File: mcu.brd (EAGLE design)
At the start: 36.7 x 57.5 mm, 64 parts, among them IC1 MCP73831/OT, T1 SI7051-A20, U4 NRF52832, U7 CP2102N-A01-GQFN24, X1 LFXTAL069526, X6 32.768kHz

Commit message: UPD: finishied version to macrofab
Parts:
- removed GND: (no value), microbuilder:TESTPOINT_ROUND_2MM
- moved C42 10.2 mm to (48.8, 43.6), turned to 0 degrees
- moved R9 8.40 mm to (46.0, 64.1), turned to 0 degrees
- moved L10 7.43 mm to (46.0, 43.9)
- moved R11 6.39 mm to (46.0, 41.3)
- moved R15 4.80 mm to (46.0, 62.1), turned to 0 degrees
- moved L9 3.90 mm to (45.4, 46.4), turned to 270 degrees
- moved DFU 3.70 mm to (49.1, 64.3)
- moved R12 1.05 mm to (44.1, 54.0), turned to 90 degrees
- moved X6 0.89 mm to (48.2, 45.7)
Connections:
- net GND: no longer GND.P$1
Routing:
- net DEC4: track 4.97 -> 16.2 mm
- net P0.26: track 59.8 -> 68.2 mm
- net VBAT: track 43.9 -> 37.1 mm
- net P0.31: track 16.5 -> 20.3 mm
- net P0.25: track 61.9 -> 65.7 mm
- net N$10: track 5.60 -> 7.61 mm
- net P0.20: track 13.2 -> 12.4 mm
- net P0.01/XL2: track 5.94 -> 6.67 mm
- net V+: track 95.4 -> 94.7 mm
- net GND: vias 101 -> 103
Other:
- board size 36.7 x 57.5 mm -> 35.5 x 57 mm
- board text removed: "GND"

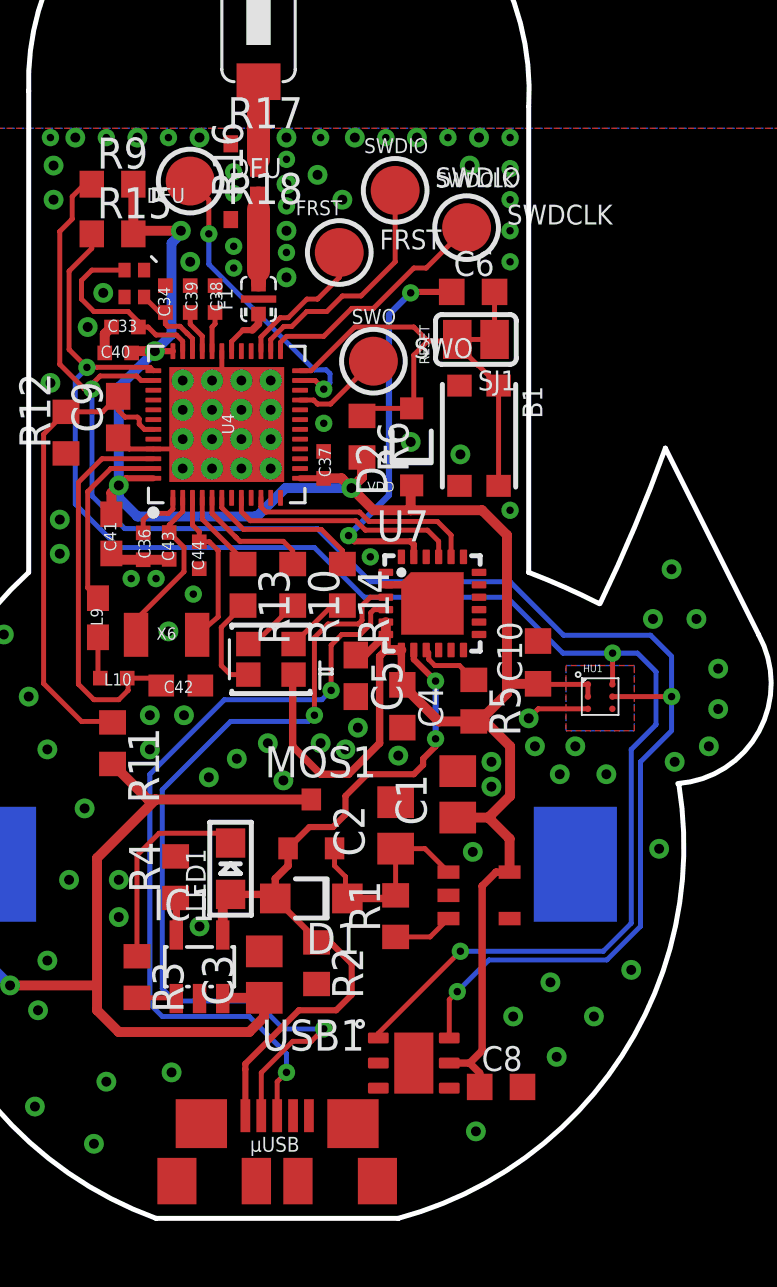
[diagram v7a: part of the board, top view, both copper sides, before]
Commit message: FIX: txd, rxd lines, usb. UPD: testpoints.
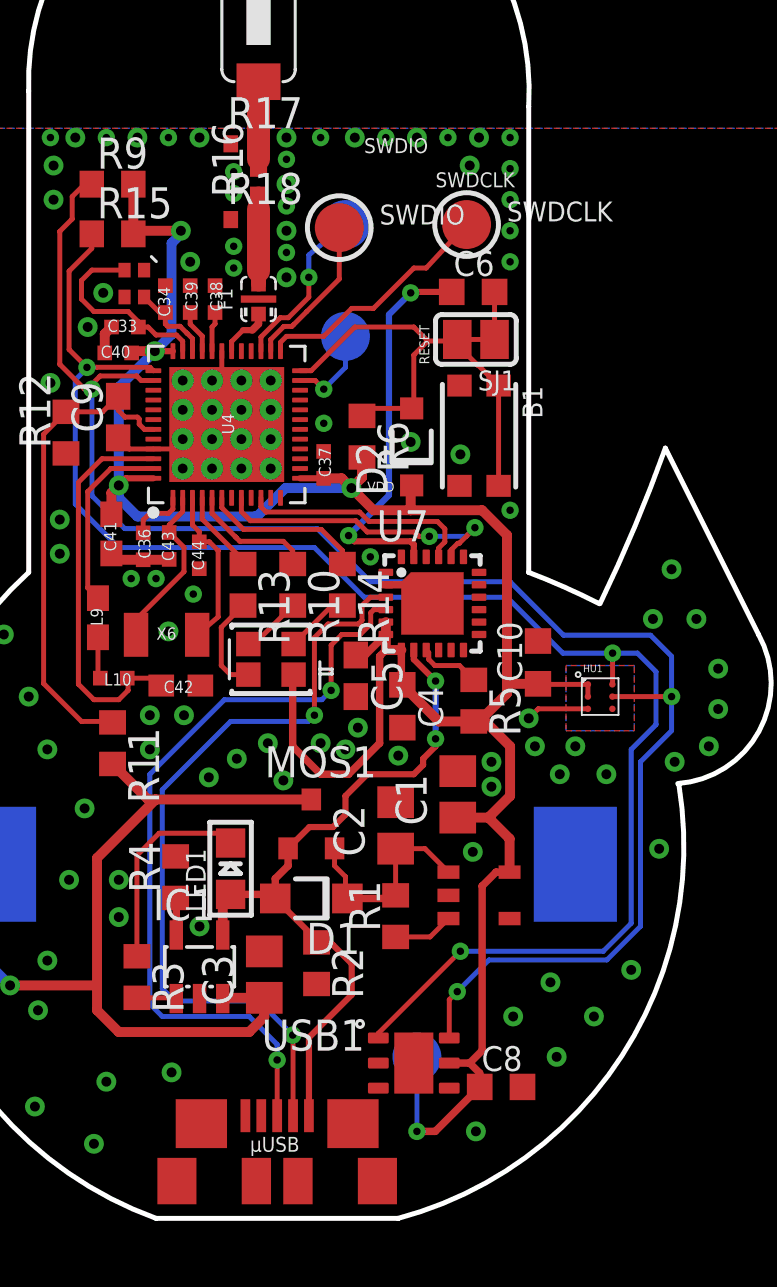
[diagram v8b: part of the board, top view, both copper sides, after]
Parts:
- moved SWO 28.5 mm to (58.4, 28.4), flipped to the bottom
- moved DFU 8.98 mm to (55.5, 57.9), flipped to the bottom
- moved SWDIO 2.75 mm to (55.2, 62.4)
- moved FRST 1.17 mm to (55.5, 62.5), flipped to the bottom
- moved SWDCLK 0.13 mm to (60.5, 62.5)
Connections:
- net P0.18/SWO: no longer SWO.P$1
- net RXD: now also U7.21; no longer U7.20
- net TXD: now also U7.20; no longer U7.21
- net V+: now also SWO.P$1
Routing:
- net P0.20: track 12.4 -> 3.64 mm, vias 2 -> 1
- net V+: track 94.7 -> 101.1 mm, vias 4 -> 5
- net P0.18/SWO: track 3.79 -> 0.00 mm
- net SWDIO: track 9.80 -> 6.40 mm
- net USBD+: track 35.1 -> 32.2 mm
- net TXD: track 9.77 -> 12.3 mm, vias 0 -> 2
- net VUSB: track 32.2 -> 30.3 mm
- net P0.22: track 5.81 -> 6.88 mm, vias 0 -> 1
- net GND: vias 103 -> 101
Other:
- board text added: "3.3V"
- board text added: "TilesTemp v2.0 ISSE-IDI-NTNU Trondheim Francesco Gianni Monica Divitini Welle Design"
- board text removed: "SWO"
- board text removed: "TilesTemp v1.0 ISSE-IDI-NTNU Trondheim Francesco Gianni, Monica Divitini Welle Design"
